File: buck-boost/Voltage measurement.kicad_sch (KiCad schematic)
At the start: 0 parts

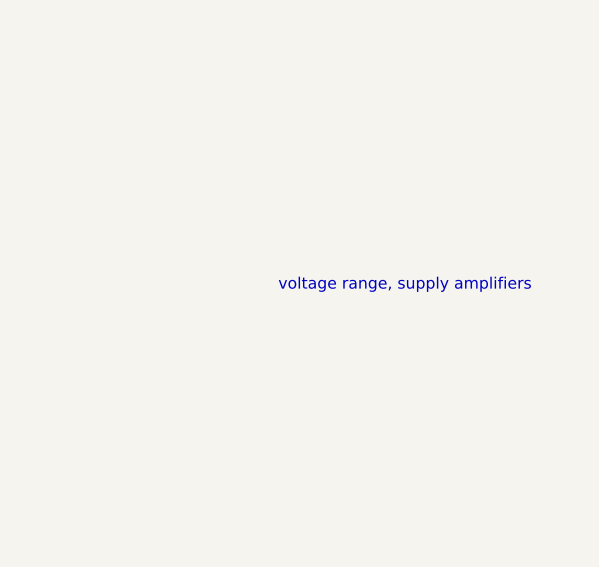
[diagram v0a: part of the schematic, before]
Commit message: Adding supply block
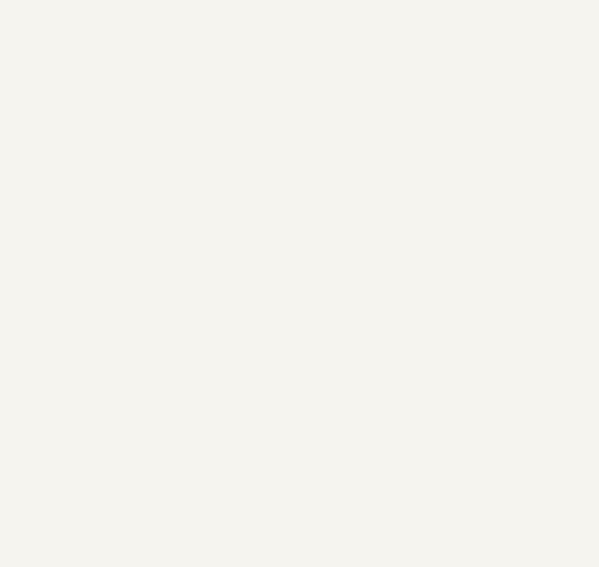
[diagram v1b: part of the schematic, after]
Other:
- note removed: "voltage range, supply amplifiers"
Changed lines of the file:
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@@
-		)
-	)
-	(text "voltage range, supply amplifiers"
-		(exclude_from_sim no)
-		(at 194.056 151.638 0)
-		(effects
-			(font
-				(size 1.27 1.27)
-			)
 		)
 	)

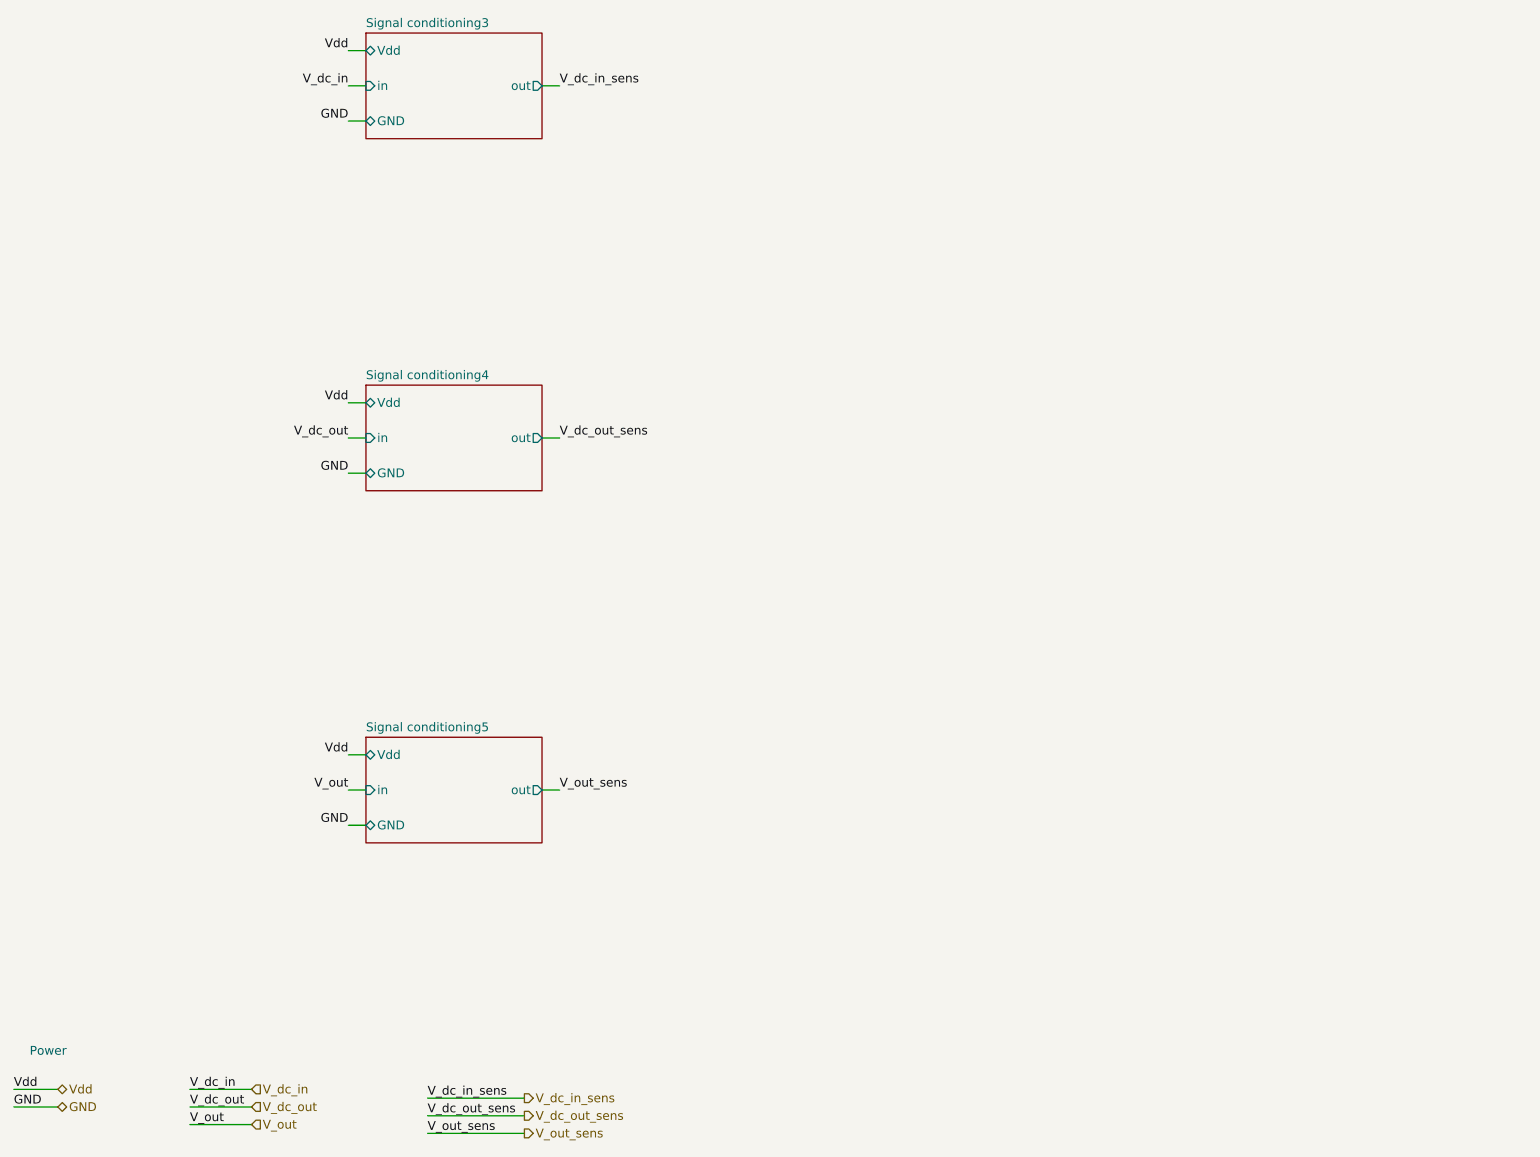
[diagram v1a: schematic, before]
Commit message: The changes indicated in the text document Review. 05.11.2024 were implemented. Missing footprints were added
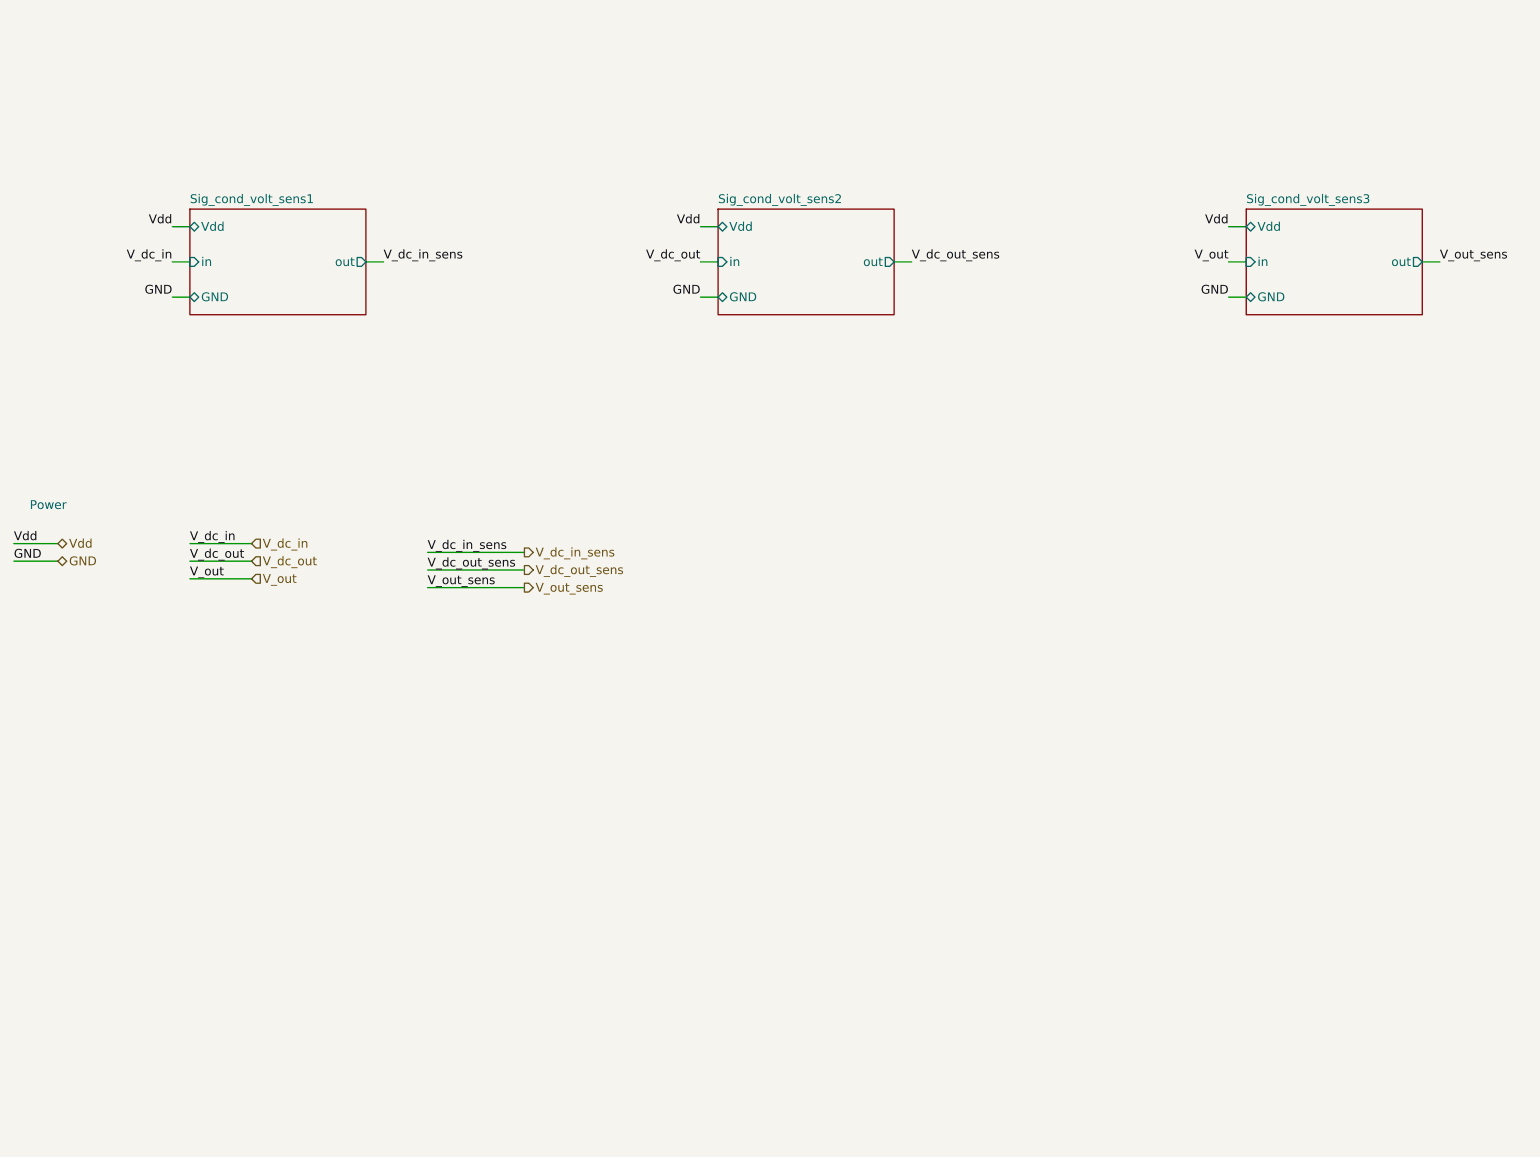
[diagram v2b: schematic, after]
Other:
- sheet Signal conditioning3 renamed Sig_cond_volt_sens1
- sheet Signal conditioning4 renamed Sig_cond_volt_sens2
- sheet Signal conditioning5 renamed Sig_cond_volt_sens3
- sheet Sig_cond_volt_sens1: file Signal conditioning3.kicad_sch -> Signal conditioning_Voltage.kicad_sch
- sheet Sig_cond_volt_sens2: file Signal conditioning3.kicad_sch -> Signal conditioning_Voltage.kicad_sch
- sheet Sig_cond_volt_sens3: file Signal conditioning3.kicad_sch -> Signal conditioning_Voltage.kicad_sch
